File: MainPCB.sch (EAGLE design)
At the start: 0 parts

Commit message: put on STM
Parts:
- added U$1: STM32F410R8T6, SeniorDesignParts:STM32F410R8T6
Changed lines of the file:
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@@
 <parts>
 <part name="FRAME1" library="SparkFun-Aesthetics" library_urn="urn:adsk.eagle:library:507" deviceset="FRAME-A4L" device=""/>
+<part name="U$1" library="SeniorDesignParts" deviceset="STM32F410R8T6" device=""/>
 </parts>
 <sheets>
@@
 <attribute name="SHEET" x="195.58" y="1.27" size="2.54" layer="94" font="vector"/>
 </instance>
+<instance part="U$1" gate="G$1" x="78.74" y="93.98"/>
 </instances>
 <busses>

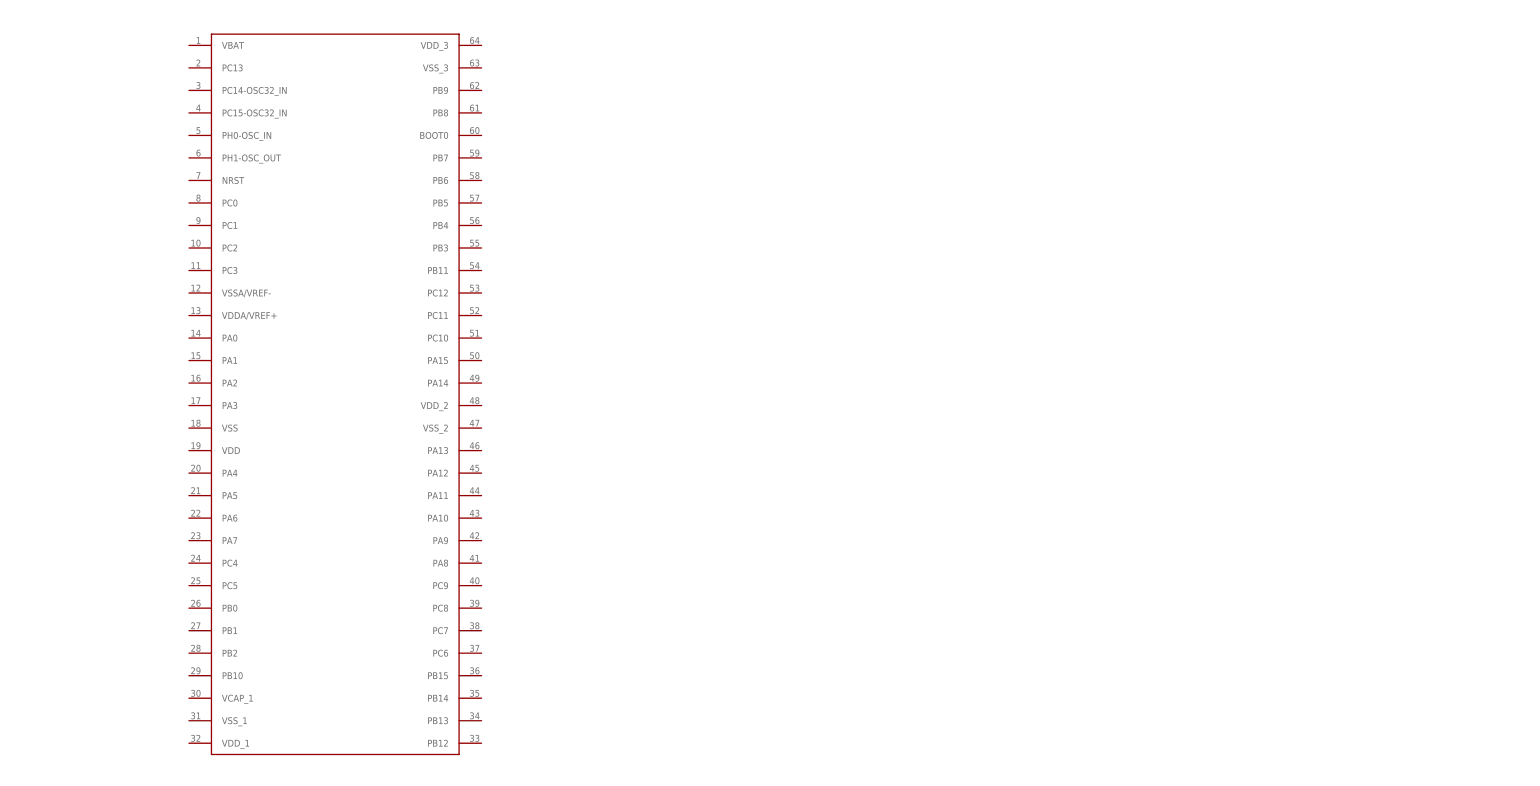
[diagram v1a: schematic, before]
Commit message: added LCD connector
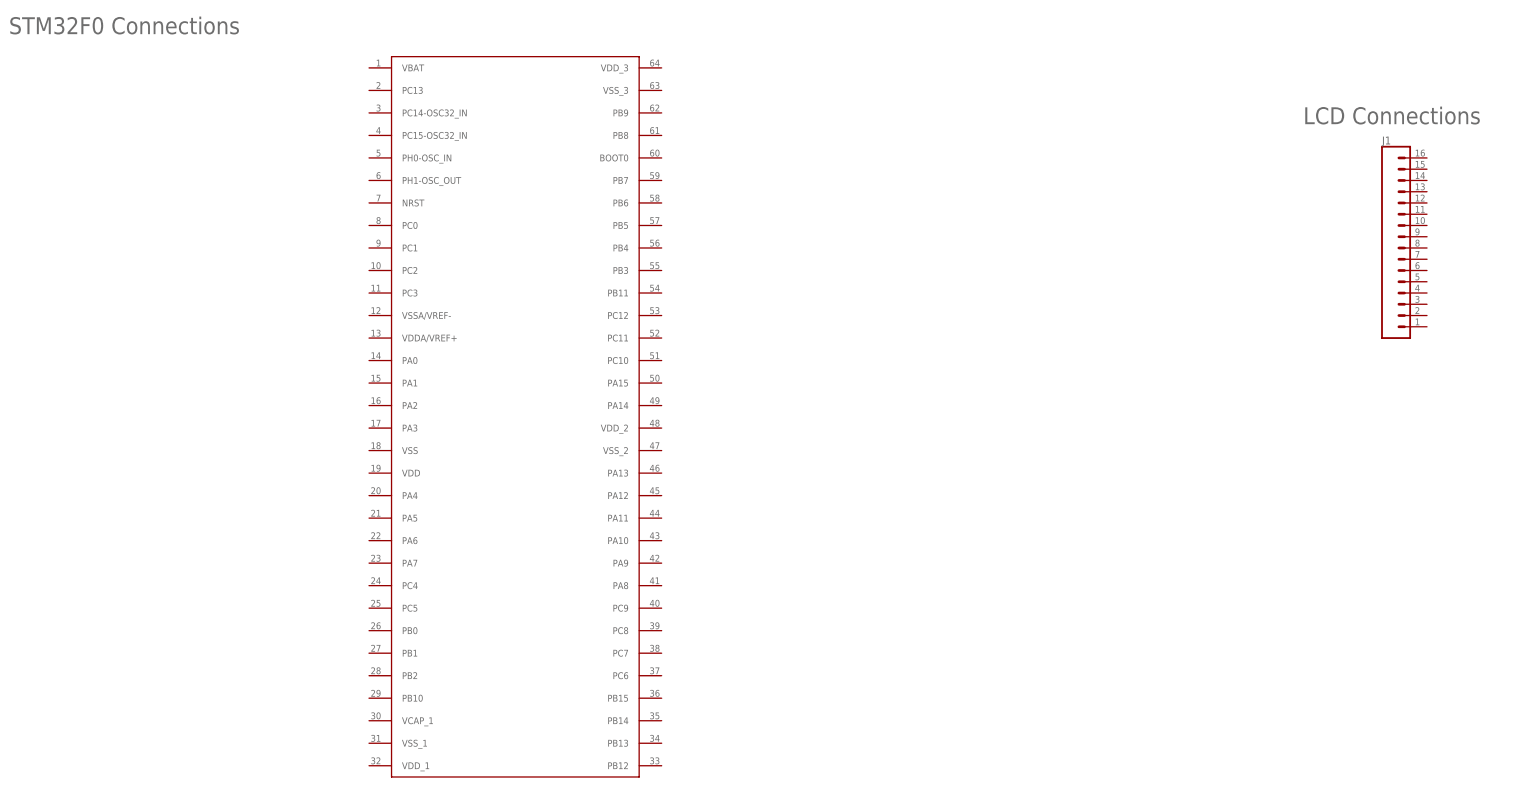
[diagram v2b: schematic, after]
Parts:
- added J1: (no value), SparkFun-Connectors:CONN_161X16_NO_SILK
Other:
- note added: "LCD Connections"
- note added: "STM32F0 Connections"
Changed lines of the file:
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@@
 <layer number="230" name="230bmp" color="7" fill="1" visible="yes" active="yes"/>
 <layer number="231" name="231bmp" color="7" fill="1" visible="yes" active="yes"/>
+<layer number="232" name="Eagle3D_PG2" color="7" fill="1" visible="yes" active="yes"/>
+<layer number="233" name="Eagle3D_PG3" color="7" fill="1" visible="yes" active="yes"/>
 <layer number="248" name="Housing" color="7" fill="1" visible="yes" active="yes"/>
 <layer number="249" name="Edge" color="7" fill="1" visible="yes" active="yes"/>
@@
 <part name="FRAME1" library="SparkFun-Aesthetics" library_urn="urn:adsk.eagle:library:507" deviceset="FRAME-A4L" device=""/>
 <part name="U$1" library="SeniorDesignParts" deviceset="STM32F410R8T6" device=""/>
+<part name="J1" library="SparkFun-Connectors" library_urn="urn:adsk.eagle:library:513" deviceset="CONN_16" device="1X16_NO_SILK" package3d_urn="urn:adsk.eagle:package:38249/1"/>
+<part name="FRAME2" library="SparkFun-Aesthetics" library_urn="urn:adsk.eagle:library:507" deviceset="FRAME-A4L" device=""/>
 </parts>
 <sheets>
 <sheet>
 <plain>
+<text x="5.08" y="172.72" size="3.81" layer="95">STM32F0 Connections</text>
+<text x="297.18" y="152.4" size="3.81" layer="95">LCD Connections</text>
 </plain>
 <instances>
@@
 <attribute name="SHEET" x="195.58" y="1.27" size="2.54" layer="94" font="vector"/>
 </instance>
-<instance part="U$1" gate="G$1" x="78.74" y="93.98"/>
+<instance part="U$1" gate="G$1" x="119.38" y="88.9"/>
+<instance part="J1" gate="G$1" x="314.96" y="127">
+<attribute name="VALUE" x="314.96" y="101.854" size="1.778" layer="96" font="vector"/>
+<attribute name="NAME" x="314.96" y="147.828" size="1.778" layer="95" font="vector"/>
+</instance>
+<instance part="FRAME2" gate="G$1" x="281.94" y="0">
+<attribute name="DRAWING_NAME" x="463.55" y="11.43" size="2.54" layer="94" font="vector"/>
+<attribute name="LAST_DATE_TIME" x="463.55" y="6.35" size="2.286" layer="94" font="vector"/>
+<attribute name="SHEET" x="477.52" y="1.27" size="2.54" layer="94" font="vector"/>
+</instance>
 </instances>
 <busses>
@@
 will not be understood (or retained) with this version.
 </note>
+<note version="8.3" severity="warning">
+Since Version 8.3, EAGLE supports the association of 3D packages
+with devices in libraries, schematics, and board files. Those 3D
+packages will not be understood (or retained) with this version.
+</note>
 </compatibility>

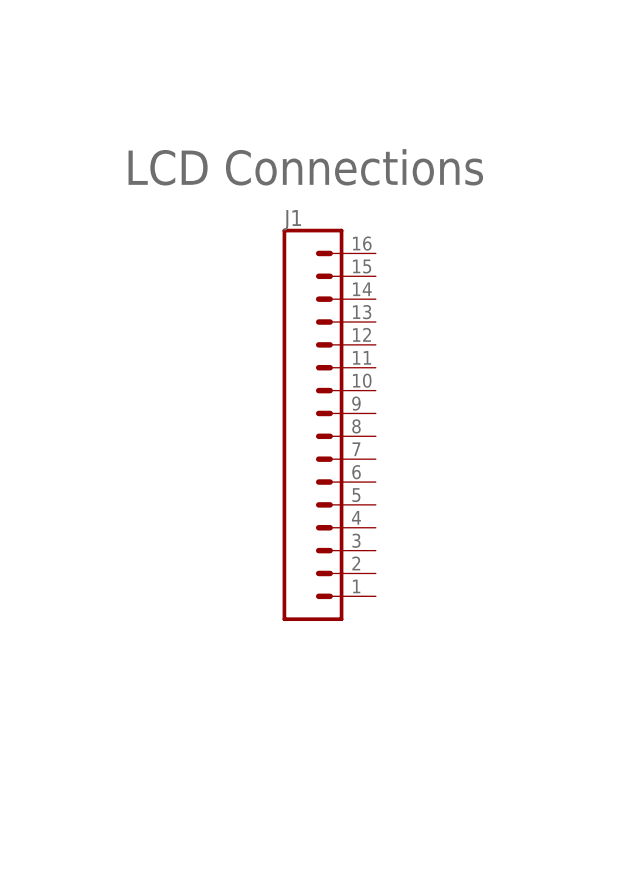
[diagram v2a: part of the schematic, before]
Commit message: added lcd connections
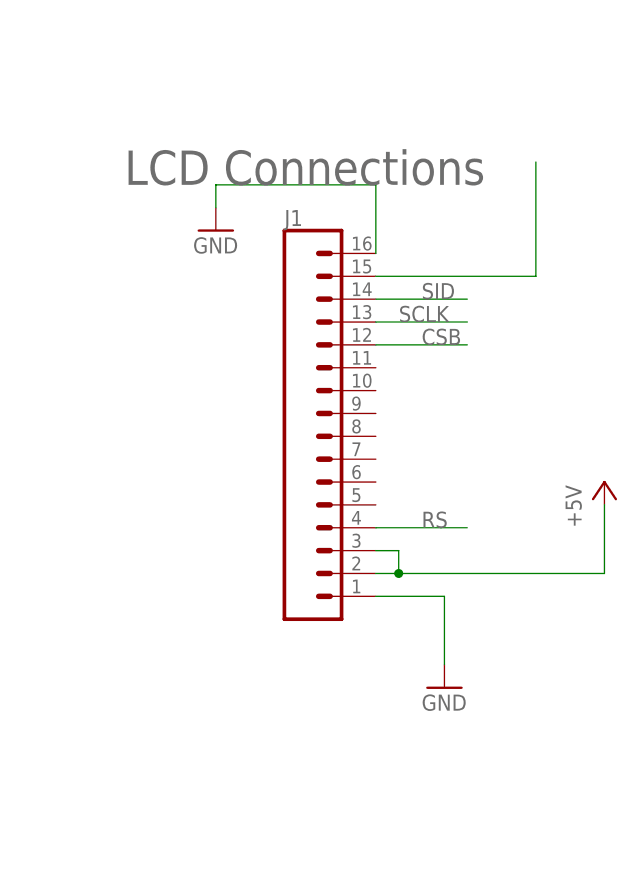
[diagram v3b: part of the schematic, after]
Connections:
- new net +5V: J1.2, J1.3
- new net CSB: J1.12
- new net GND: J1.1, J1.16
- new net N$1: J1.15
- new net RS: J1.4
- new net SCLK: J1.13
- new net SID: J1.14
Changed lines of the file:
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@@
 <layers>
 <layer number="1" name="Top" color="4" fill="1" visible="no" active="no"/>
+<layer number="2" name="Route2" color="1" fill="3" visible="no" active="no"/>
+<layer number="3" name="Route3" color="4" fill="3" visible="no" active="no"/>
+<layer number="4" name="Route4" color="1" fill="4" visible="no" active="no"/>
+<layer number="5" name="Route5" color="4" fill="4" visible="no" active="no"/>
+<layer number="6" name="Route6" color="1" fill="8" visible="no" active="no"/>
+<layer number="7" name="Route7" color="4" fill="8" visible="no" active="no"/>
+<layer number="8" name="Route8" color="1" fill="2" visible="no" active="no"/>
+<layer number="9" name="Route9" color="4" fill="2" visible="no" active="no"/>
+<layer number="10" name="Route10" color="1" fill="7" visible="no" active="no"/>
+<layer number="11" name="Route11" color="4" fill="7" visible="no" active="no"/>
+<layer number="12" name="Route12" color="1" fill="5" visible="no" active="no"/>
+<layer number="13" name="Route13" color="4" fill="5" visible="no" active="no"/>
+<layer number="14" name="Route14" color="1" fill="6" visible="no" active="no"/>
+<layer number="15" name="Route15" color="4" fill="6" visible="no" active="no"/>
 <layer number="16" name="Bottom" color="1" fill="1" visible="no" active="no"/>
 <layer number="17" name="Pads" color="2" fill="1" visible="no" active="no"/>
@@
 <part name="J1" library="SparkFun-Connectors" library_urn="urn:adsk.eagle:library:513" deviceset="CONN_16" device="1X16_NO_SILK" package3d_urn="urn:adsk.eagle:package:38249/1"/>
 <part name="FRAME2" library="SparkFun-Aesthetics" library_urn="urn:adsk.eagle:library:507" deviceset="FRAME-A4L" device=""/>
+<part name="GND1" library="supply1" library_urn="urn:adsk.eagle:library:371" deviceset="GND" device=""/>
+<part name="P+1" library="supply1" library_urn="urn:adsk.eagle:library:371" deviceset="+5V" device=""/>
+<part name="GND2" library="supply1" library_urn="urn:adsk.eagle:library:371" deviceset="GND" device=""/>
 </parts>
 <sheets>
@@
 <attribute name="SHEET" x="477.52" y="1.27" size="2.54" layer="94" font="vector"/>
 </instance>
+<instance part="GND1" gate="1" x="332.74" y="96.52">
+<attribute name="VALUE" x="330.2" y="93.98" size="1.778" layer="96"/>
+</instance>
+<instance part="P+1" gate="1" x="350.52" y="119.38">
+<attribute name="VALUE" x="347.98" y="114.3" size="1.778" layer="96" rot="R90"/>
+</instance>
+<instance part="GND2" gate="1" x="307.34" y="147.32">
+<attribute name="VALUE" x="304.8" y="144.78" size="1.778" layer="96"/>
+</instance>
 </instances>
 <busses>
 </busses>
 <nets>
+<net name="GND" class="0">
+<segment>
+<pinref part="J1" gate="G$1" pin="1"/>
+<wire x1="325.12" y1="106.68" x2="332.74" y2="106.68" width="0.1524" layer="91"/>
+<wire x1="332.74" y1="106.68" x2="332.74" y2="99.06" width="0.1524" layer="91"/>
+<pinref part="GND1" gate="1" pin="GND"/>
+</segment>
+<segment>
+<pinref part="J1" gate="G$1" pin="16"/>
+<wire x1="325.12" y1="144.78" x2="325.12" y2="152.4" width="0.1524" layer="91"/>
+<wire x1="325.12" y1="152.4" x2="307.34" y2="152.4" width="0.1524" layer="91"/>
+<wire x1="307.34" y1="152.4" x2="307.34" y2="149.86" width="0.1524" layer="91"/>
+<pinref part="GND2" gate="1" pin="GND"/>
+</segment>
+</net>
+<net name="+5V" class="0">
+<segment>
+<pinref part="J1" gate="G$1" pin="2"/>
+<wire x1="325.12" y1="109.22" x2="327.66" y2="109.22" width="0.1524" layer="91"/>
+<wire x1="327.66" y1="109.22" x2="350.52" y2="109.22" width="0.1524" layer="91"/>
+<wire x1="350.52" y1="109.22" x2="350.52" y2="116.84" width="0.1524" layer="91"/>
+<pinref part="P+1" gate="1" pin="+5V"/>
+<pinref part="J1" gate="G$1" pin="3"/>
+<wire x1="325.12" y1="111.76" x2="327.66" y2="111.76" width="0.1524" layer="91"/>
+<wire x1="327.66" y1="111.76" x2="327.66" y2="109.22" width="0.1524" layer="91"/>
+<junction x="327.66" y="109.22"/>
+</segment>
+</net>
+<net name="RS" class="0">
+<segment>
+<pinref part="J1" gate="G$1" pin="4"/>
+<wire x1="325.12" y1="114.3" x2="335.28" y2="114.3" width="0.1524" layer="91"/>
+<label x="330.2" y="114.3" size="1.778" layer="95"/>
+</segment>
+</net>
+<net name="CSB" class="0">
+<segment>
+<pinref part="J1" gate="G$1" pin="12"/>
+<wire x1="325.12" y1="134.62" x2="335.28" y2="134.62" width="0.1524" layer="91"/>
+<label x="330.2" y="134.62" size="1.778" layer="95"/>
+</segment>
+</net>
+<net name="SCLK" class="0">
+<segment>
+<pinref part="J1" gate="G$1" pin="13"/>
+<wire x1="325.12" y1="137.16" x2="335.28" y2="137.16" width="0.1524" layer="91"/>
+<label x="327.66" y="137.16" size="1.778" layer="95"/>
+</segment>
+</net>
+<net name="SID" class="0">
+<segment>
+<pinref part="J1" gate="G$1" pin="14"/>
+<wire x1="325.12" y1="139.7" x2="335.28" y2="139.7" width="0.1524" layer="91"/>
+<label x="330.2" y="139.7" size="1.778" layer="95"/>
+</segment>
+</net>
+<net name="N$1" class="0">
+<segment>
+<pinref part="J1" gate="G$1" pin="15"/>
+<wire x1="325.12" y1="142.24" x2="342.9" y2="142.24" width="0.1524" layer="91"/>
+<wire x1="342.9" y1="142.24" x2="342.9" y2="154.94" width="0.1524" layer="91"/>
+</segment>
+</net>
 </nets>
 </sheet>

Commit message: started building the circuits
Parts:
- added C1, C2: 10uF, SparkFun-Capacitors:10UF-0805-10V-10%
- added C3: 100uF, SparkFun-Capacitors:100UF-POLAR-25V-20%(ELEC)
- added C4: 1000uF, SparkFun-Capacitors:100UF-POLAR-25V-20%(ELEC)
- added U$2: MFRC522, SeniorDesignParts:MFRC522
- added U$3: LM2576, SeniorDesignParts:LM2576
- added U$4: AP7363, SeniorDesignParts:AP7363
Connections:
- new net 3.3V: C2.1, J1.15, U$4.VOUT
- net +5V: now also C1.1, U$4.VIN
- net GND: now also C1.2, C2.2, U$4.GND
- net N$1: now also U$3.GND, U$3.ON/OFF; no longer J1.15

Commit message: added connections
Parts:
- added J2: DCJ0202, con-jack:DCJ0202
- added U$5: DR73-101-R, SeniorDesignParts:DR73-101-R
- added U$6: V3F6-M3/H, SeniorDesignParts:V3F6-M3/H
- added U$7: ESP32, SeniorDesignParts:ESP32
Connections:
- removed net N$1: U$3.GND, U$3.ON/OFF
- new net 9V: C3.+, J2.1, U$3.+VIN
- new net N$3: U$3.VOUT, U$5.2, U$6.A
- net +5V: now also C4.+, U$3.FEEDBACK, U$5.1
- net 3.3V: now also U$7.3V3
- net GND: now also C3.-, C4.-, J2.2, J2.3, U$2.GND, U$3.GND, U$3.ON/OFF, U$6.C, U$7.GND1, U$7.GND2, U$7.GND3, U$7.P_GND
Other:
- moved on the sheet: C1, C2, C4
